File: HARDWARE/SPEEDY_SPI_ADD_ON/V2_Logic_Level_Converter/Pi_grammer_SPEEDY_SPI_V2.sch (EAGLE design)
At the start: 11 parts, among them J2 TARGET_copy

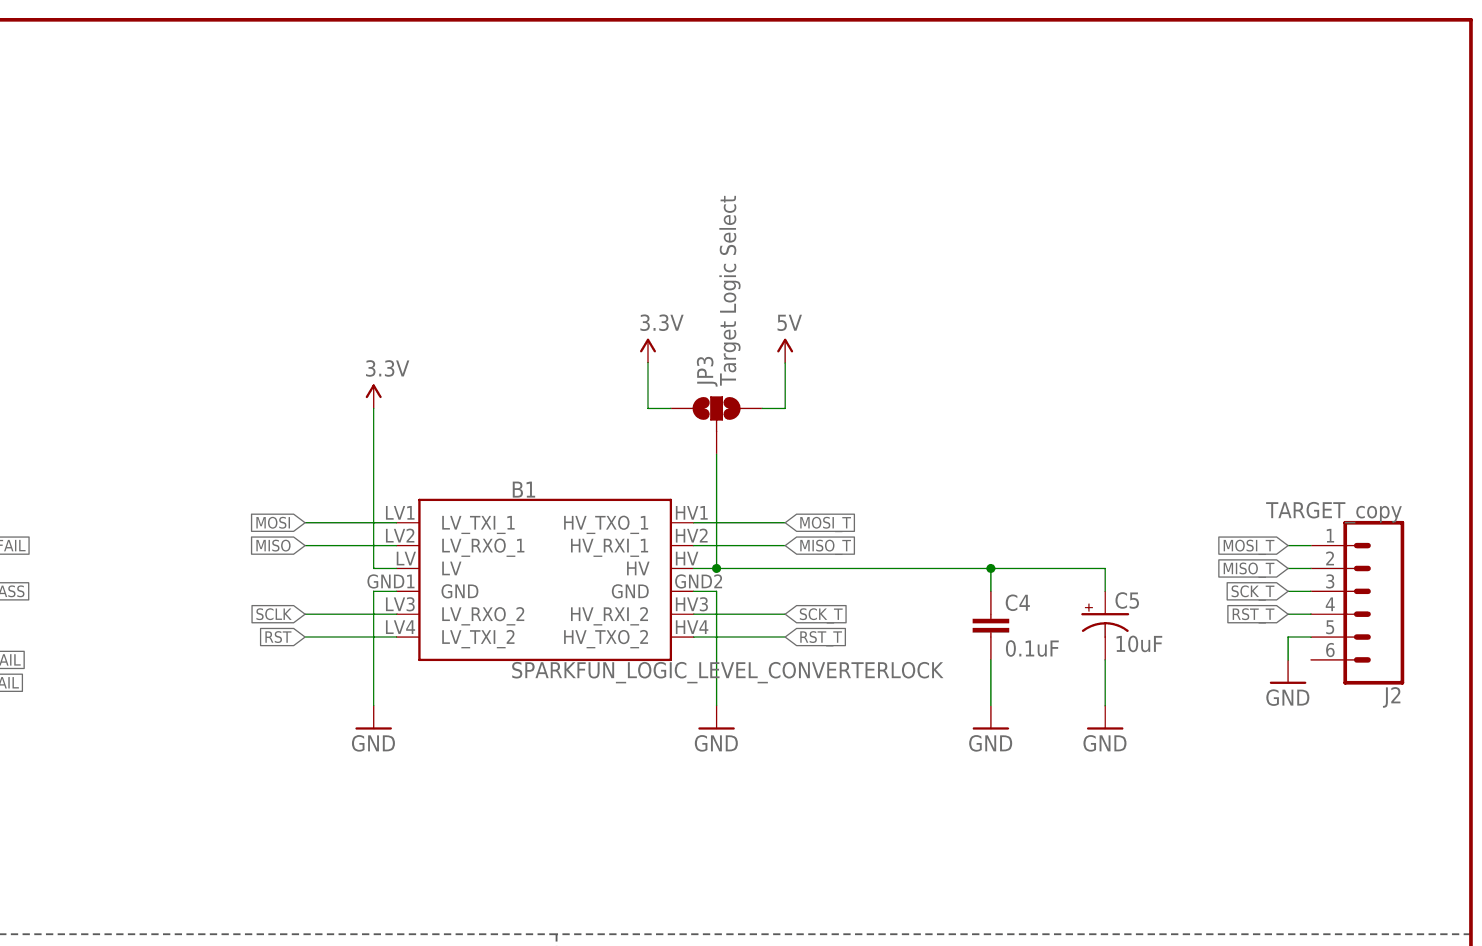
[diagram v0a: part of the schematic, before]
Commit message: Option to "tap" logic level from target
Note, this required a modification to the ADAPTER as well. I am
utilizing pin 6 on the 1x6 pin header (jumper wire) to transfer VCC back
to the logic level converter.

I'm not sure why on the original design I didn't think to include VCC in
the comm lines to the target - I think it was because the raspi doesn't
have any ADCs to actually  verify it, so I didn't know if it was worth
it.
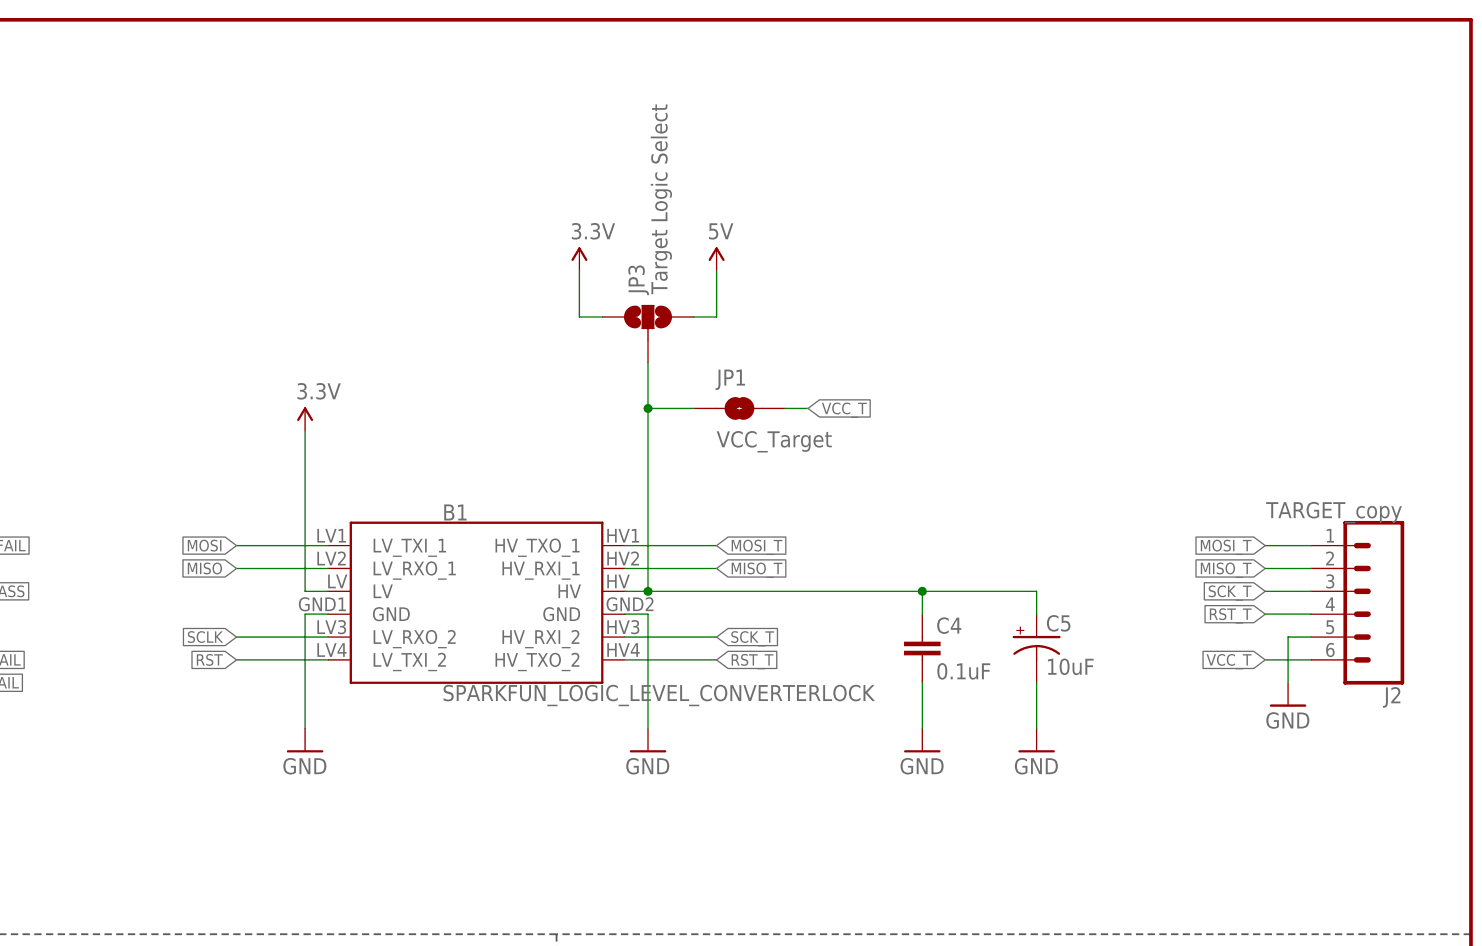
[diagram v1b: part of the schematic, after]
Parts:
- added JP1: VCC_Target, SparkFun-Jumpers:JUMPER-SMT_2_NO_SILK
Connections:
- new net VCC_T: J2.6, JP1.2
- net N$4: now also JP1.1
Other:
- moved on the sheet: B1, C4, C5, JP3

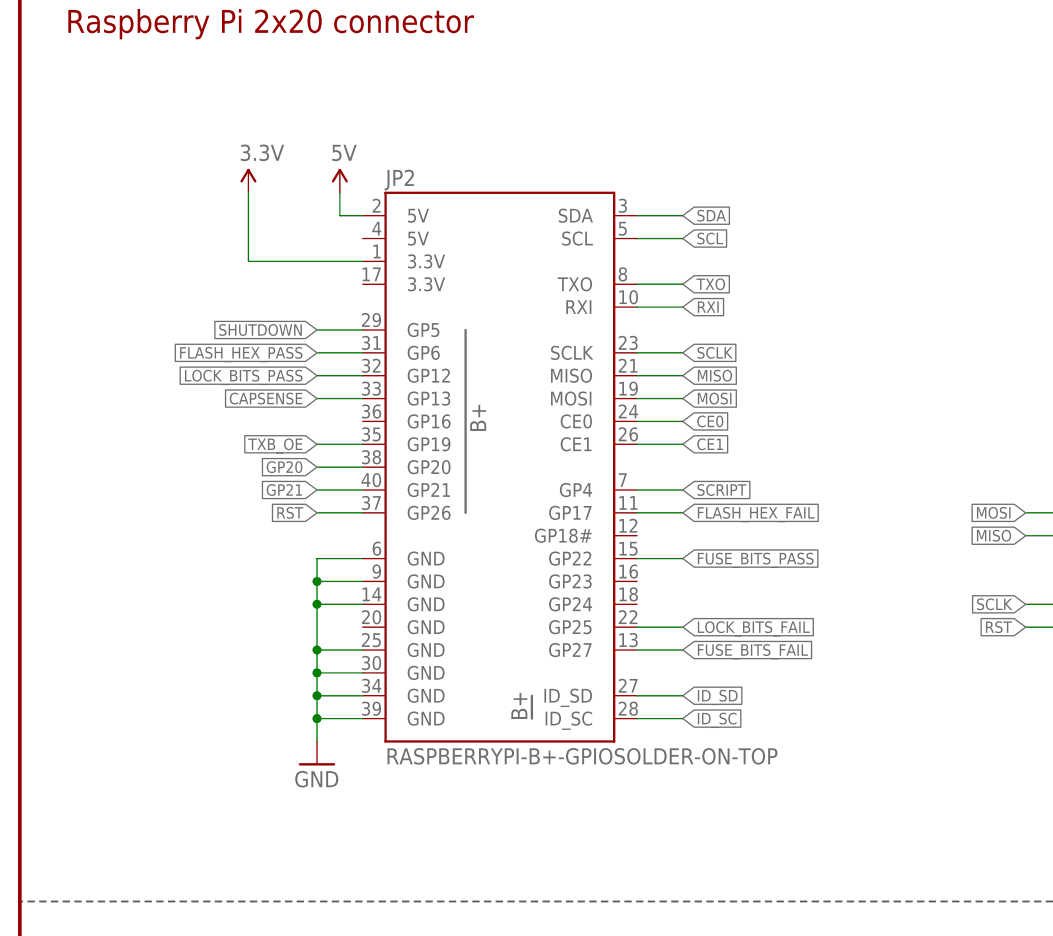
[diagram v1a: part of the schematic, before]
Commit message: Speedy SPI library work
updated device to only include pins/pads that are used. added in actual
drill hits for the unused pads.

rduced down to only 2 GND connections.

reduce isolate to 10 mils to allow for GND flow across header pins.
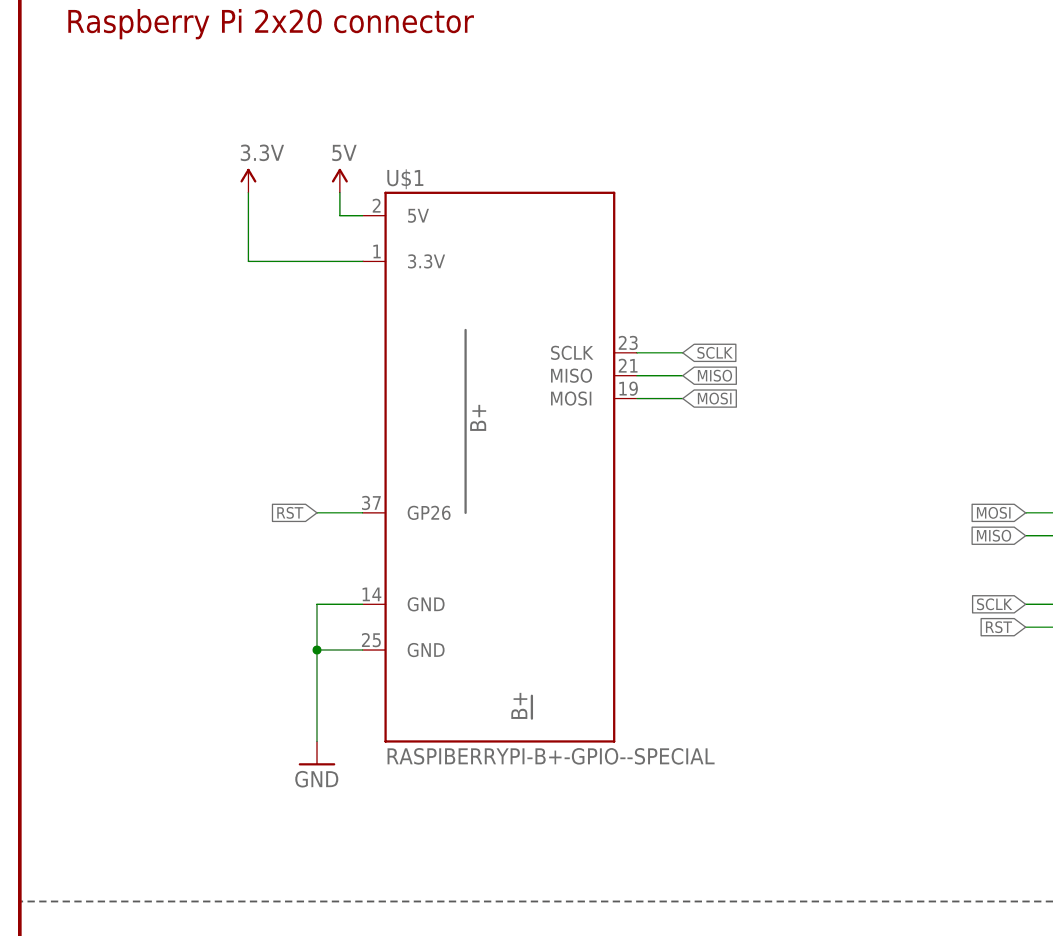
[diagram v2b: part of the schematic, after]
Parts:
- removed JP2: RASPBERRYPI-B+-GPIOSOLDER-ON-TOP, SparkFun-Boards:RASPBERRYPI-B+-GPIOSOLDER-ON-TOP
- added U$1: RASPIBERRYPI-B+-GPIO--SPECIAL, SparkFun-Boards:RASPIBERRYPI-B+-GPIO--SPECIAL
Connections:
- removed net CAPSENSE: JP2.GP13
- removed net CE0: JP2.CE0
- removed net CE1: JP2.CE1
- removed net FLASH_HEX_FAIL: JP2.GP17
- removed net FLASH_HEX_PASS: JP2.GP6
- removed net FUSE_BITS_FAIL: JP2.GP27
- removed net FUSE_BITS_PASS: JP2.GP22
- removed net GP20: JP2.GP20
- removed net GP21: JP2.GP21
- removed net ID_SC: JP2.ID_SC
- removed net ID_SD: JP2.ID_SD
- removed net LOCK_BITS_FAIL: JP2.GP25
- removed net LOCK_BITS_PASS: JP2.GP12
- removed net RXI: JP2.RXI
- removed net SCL: JP2.SCL
- removed net SCRIPT: JP2.GP4
- removed net SDA: JP2.SDA
- removed net SHUTDOWN: JP2.GP5
- removed net TXB_OE: JP2.GP19
- removed net TXO: JP2.TXO
- net 3.3V: now also U$1.3.3V@1; no longer JP2.3.3V@1
- net 5V: now also U$1.5V@2; no longer JP2.5V@2
- net GND: now also U$1.GND@14, U$1.GND@25; no longer JP2.GND@14, JP2.GND@25, JP2.GND@30, JP2.GND@34, JP2.GND@39, JP2.GND@6, JP2.GND@9
- net MISO: now also U$1.MISO; no longer JP2.MISO
- net MOSI: now also U$1.MOSI; no longer JP2.MOSI
- net RST: now also U$1.GP26; no longer JP2.GP26
- net SCLK: now also U$1.SCLK; no longer JP2.SCLK

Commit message: moved 1x6 header to allow for RA header
This should allow for the cable to flow directly downward from the
pi_grammer and sit with a lower profile. This should help prevent the
cable/header from getting knocked around during handling.

Also had to update the adapter - rotated header 180 degrees so it will
mate straight pin-to-pin on the 1x6 header on the speedySPI.
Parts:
- J2: device SparkFun-Connectors:CONN_06POLAR_LOCK -> SparkFun-Connectors:CONN_06SIP_LOCK
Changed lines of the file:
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@@
 <grid distance="0.1" unitdist="inch" unit="inch" style="lines" multiple="1" display="no" altdistance="0.01" altunitdist="inch" altunit="inch"/>
 <layers>
-<layer number="1" name="Top" color="4" fill="1" visible="no" active="no"/>
-<layer number="2" name="Route2" color="1" fill="3" visible="no" active="no"/>
-<layer number="3" name="Route3" color="4" fill="3" visible="no" active="no"/>
-<layer number="4" name="Route4" color="1" fill="4" visible="no" active="no"/>
-<layer number="5" name="Route5" color="4" fill="4" visible="no" active="no"/>
-<layer number="6" name="Route6" color="1" fill="8" visible="no" active="no"/>
-<layer number="7" name="Route7" color="4" fill="8" visible="no" active="no"/>
-<layer number="8" name="Route8" color="1" fill="2" visible="no" active="no"/>
-<layer number="9" name="Route9" color="4" fill="2" visible="no" active="no"/>
-<layer number="10" name="Route10" color="1" fill="7" visible="no" active="no"/>
-<layer number="11" name="Route11" color="4" fill="7" visible="no" active="no"/>
-<layer number="12" name="Route12" color="1" fill="5" visible="no" active="no"/>
-<layer number="13" name="Route13" color="4" fill="5" visible="no" active="no"/>
-<layer number="14" name="Route14" color="1" fill="6" visible="no" active="no"/>
-<layer number="15" name="Route15" color="4" fill="6" visible="no" active="no"/>
-<layer number="16" name="Bottom" color="1" fill="1" visible="no" active="no"/>
-<layer number="17" name="Pads" color="2" fill="1" visible="no" active="no"/>
-<layer number="18" name="Vias" color="2" fill="1" visible="no" active="no"/>
-<layer number="19" name="Unrouted" color="6" fill="1" visible="no" active="no"/>
-<layer number="20" name="Dimension" color="15" fill="1" visible="no" active="no"/>
-<layer number="21" name="tPlace" color="16" fill="1" visible="no" active="no"/>
-<layer number="22" name="bPlace" color="14" fill="1" visible="no" active="no"/>
-<layer number="23" name="tOrigins" color="15" fill="1" visible="no" active="no"/>
-<layer number="24" name="bOrigins" color="15" fill="1" visible="no" active="no"/>
-<layer number="25" name="tNames" color="7" fill="1" visible="no" active="no"/>
-<layer number="26" name="bNames" color="7" fill="1" visible="no" active="no"/>
-<layer number="27" name="tValues" color="7" fill="1" visible="no" active="no"/>
-<layer number="28" name="bValues" color="7" fill="1" visible="no" active="no"/>
+<layer number="1" name="Top" color="4" fill="1" visible="yes" active="no"/>
+<layer number="2" name="Route2" color="1" fill="3" visible="yes" active="no"/>
+<layer number="3" name="Route3" color="4" fill="3" visible="yes" active="no"/>
+<layer number="4" name="Route4" color="1" fill="4" visible="yes" active="no"/>
+<layer number="5" name="Route5" color="4" fill="4" visible="yes" active="no"/>
+<layer number="6" name="Route6" color="1" fill="8" visible="yes" active="no"/>
+<layer number="7" name="Route7" color="4" fill="8" visible="yes" active="no"/>
+<layer number="8" name="Route8" color="1" fill="2" visible="yes" active="no"/>
+<layer number="9" name="Route9" color="4" fill="2" visible="yes" active="no"/>
+<layer number="10" name="Route10" color="1" fill="7" visible="yes" active="no"/>
+<layer number="11" name="Route11" color="4" fill="7" visible="yes" active="no"/>
+<layer number="12" name="Route12" color="1" fill="5" visible="yes" active="no"/>
+<layer number="13" name="Route13" color="4" fill="5" visible="yes" active="no"/>
+<layer number="14" name="Route14" color="1" fill="6" visible="yes" active="no"/>
+<layer number="15" name="Route15" color="4" fill="6" visible="yes" active="no"/>
+<layer number="16" name="Bottom" color="1" fill="1" visible="yes" active="no"/>
+<layer number="17" name="Pads" color="2" fill="1" visible="yes" active="no"/>
+<layer number="18" name="Vias" color="2" fill="1" visible="yes" active="no"/>
+<layer number="19" name="Unrouted" color="6" fill="1" visible="yes" active="no"/>
+<layer number="20" name="Dimension" color="15" fill="1" visible="yes" active="no"/>
+<layer number="21" name="tPlace" color="16" fill="1" visible="yes" active="no"/>
+<layer number="22" name="bPlace" color="14" fill="1" visible="yes" active="no"/>
+<layer number="23" name="tOrigins" color="15" fill="1" visible="yes" active="no"/>
+<layer number="24" name="bOrigins" color="15" fill="1" visible="yes" active="no"/>
+<layer number="25" name="tNames" color="7" fill="1" visible="yes" active="no"/>
+<layer number="26" name="bNames" color="7" fill="1" visible="yes" active="no"/>
+<layer number="27" name="tValues" color="7" fill="1" visible="yes" active="no"/>
+<layer number="28" name="bValues" color="7" fill="1" visible="yes" active="no"/>
 <layer number="29" name="tStop" color="7" fill="3" visible="no" active="no"/>
 <layer number="30" name="bStop" color="7" fill="6" visible="no" active="no"/>
@@
 <layer number="35" name="tGlue" color="7" fill="4" visible="no" active="no"/>
 <layer number="36" name="bGlue" color="7" fill="5" visible="no" active="no"/>
-<layer number="37" name="tTest" color="7" fill="1" visible="no" active="no"/>
-<layer number="38" name="bTest" color="7" fill="1" visible="no" active="no"/>
+<layer number="37" name="tTest" color="7" fill="1" visible="yes" active="no"/>
+<layer number="38" name="bTest" color="7" fill="1" visible="yes" active="no"/>
 <layer number="39" name="tKeepout" color="4" fill="11" visible="no" active="no"/>
 <layer number="40" name="bKeepout" color="1" fill="11" visible="no" active="no"/>
@@
 <layer number="44" name="Drills" color="7" fill="1" visible="no" active="no"/>
 <layer number="45" name="Holes" color="7" fill="1" visible="no" active="no"/>
-<layer number="46" name="Milling" color="3" fill="1" visible="no" active="no"/>
-<layer number="47" name="Measures" color="7" fill="1" visible="no" active="no"/>
-<layer number="48" name="Document" color="7" fill="1" visible="no" active="no"/>
-<layer number="49" name="Reference" color="13" fill="1" visible="no" active="no"/>
-<layer number="50" name="dxf" color="7" fill="1" visible="no" active="no"/>
-<layer number="51" name="tDocu" color="6" fill="1" visible="no" active="no"/>
-<layer number="52" name="bDocu" color="7" fill="1" visible="no" active="no"/>
-<layer number="53" name="tGND_GNDA" color="7" fill="9" visible="no" active="no"/>
-<layer number="54" name="bGND_GNDA" color="1" fill="9" visible="no" active="no"/>
-<layer number="56" name="wert" color="7" fill="1" visible="no" active="no"/>
-<layer number="57" name="tCAD" color="7" fill="1" visible="no" active="no"/>
-<layer number="59" name="tCarbon" color="7" fill="1" visible="no" active="no"/>
-<layer number="60" name="bCarbon" color="7" fill="1" visible="no" active="no"/>
+<layer number="46" name="Milling" color="3" fill="1" visible="yes" active="no"/>
+<layer number="47" name="Measures" color="7" fill="1" visible="yes" active="no"/>
+<layer number="48" name="Document" color="7" fill="1" visible="yes" active="no"/>
+<layer number="49" name="Reference" color="13" fill="1" visible="yes" active="no"/>
+<layer number="50" name="dxf" color="7" fill="1" visible="yes" active="no"/>
+<layer number="51" name="tDocu" color="6" fill="1" visible="yes" active="no"/>
+<layer number="52" name="bDocu" color="7" fill="1" visible="yes" active="no"/>
+<layer number="53" name="tGND_GNDA" color="7" fill="9" visible="yes" active="no"/>
+<layer number="54" name="bGND_GNDA" color="1" fill="9" visible="yes" active="no"/>
+<layer number="56" name="wert" color="7" fill="1" visible="yes" active="no"/>
+<layer number="57" name="tCAD" color="7" fill="1" visible="yes" active="no"/>
+<layer number="59" name="tCarbon" color="7" fill="1" visible="yes" active="no"/>
+<layer number="60" name="bCarbon" color="7" fill="1" visible="yes" active="no"/>
 <layer number="90" name="Modules" color="5" fill="1" visible="yes" active="yes"/>
 <layer number="91" name="Nets" color="2" fill="1" visible="yes" active="yes"/>
@@
 <part name="LOGO1" library="SparkFun-Aesthetics" deviceset="SFE_LOGO_FLAME" device=".1_INCH"/>
 <part name="LOGO2" library="SparkFun-Aesthetics" deviceset="OSHW-LOGO" device="S" value="OSHW-LOGOS"/>
-<part name="J2" library="SparkFun-Connectors" deviceset="CONN_06" device="POLAR_LOCK" value="TARGET_copy">
+<part name="J2" library="SparkFun-Connectors" deviceset="CONN_06" device="SIP_LOCK" value="TARGET_copy">
 <attribute name="PROD_ID" value="CONN-09698"/>
 </part>
